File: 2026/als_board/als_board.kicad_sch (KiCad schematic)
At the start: 18 parts, among them J1 MAIN, J2 i2c, J3 PROG, U1 GM7333, U2 ME6209A50M3G, U3 CH32V003JxMx, U4 MAX485E

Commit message: ALS finishing touches
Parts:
- added R4, R5: 5k1, Resistor_SMD:R_0603_1608Metric, symbol Device:R_Small
- added R6, R7: 10k, Resistor_SMD:R_0603_1608Metric, symbol Device:R_Small
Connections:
- net +3V3: now also R6.1, R7.1
- net +5V: now also R4.1
- net GND: now also R5.2
- net SCL: now reaches J2.2 (Pin_2), U3.6 (PC2)
- net SCL: now also R6.2
- net SDA: now reaches J2.3 (Pin_3), U3.5 (PC1)
- net SDA: now also R7.2
- net at J1.3 (Pin_3), R3.1, U4.6 (A): now also R4.2
- net at J1.2 (Pin_2), R3.2, U4.7 (B): now also R5.1
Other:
- moved on the sheet: C5, C6, J1, J2, J3, R2, R3, U3, U4

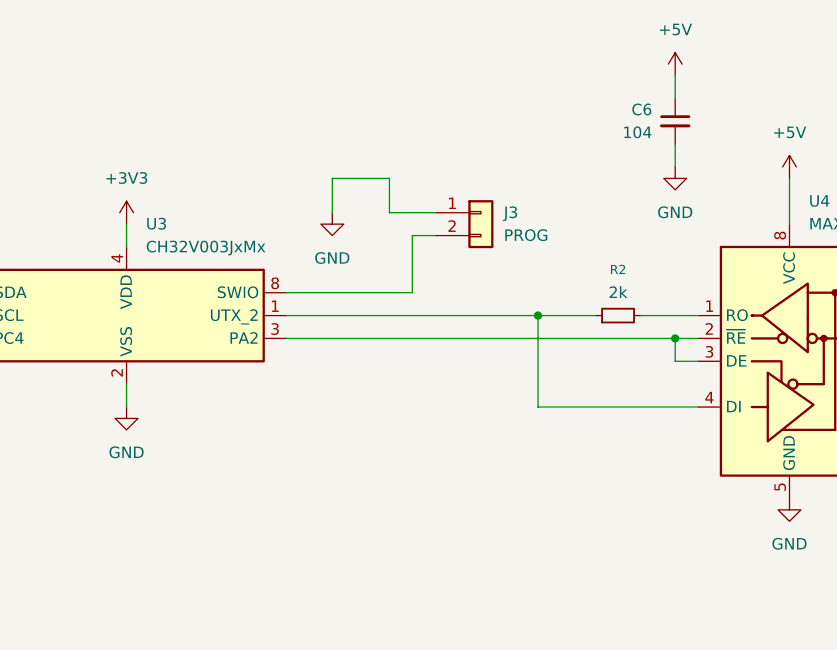
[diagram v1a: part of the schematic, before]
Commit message: ALS board with startup resistors for direction and output biasing (output off, high by default)
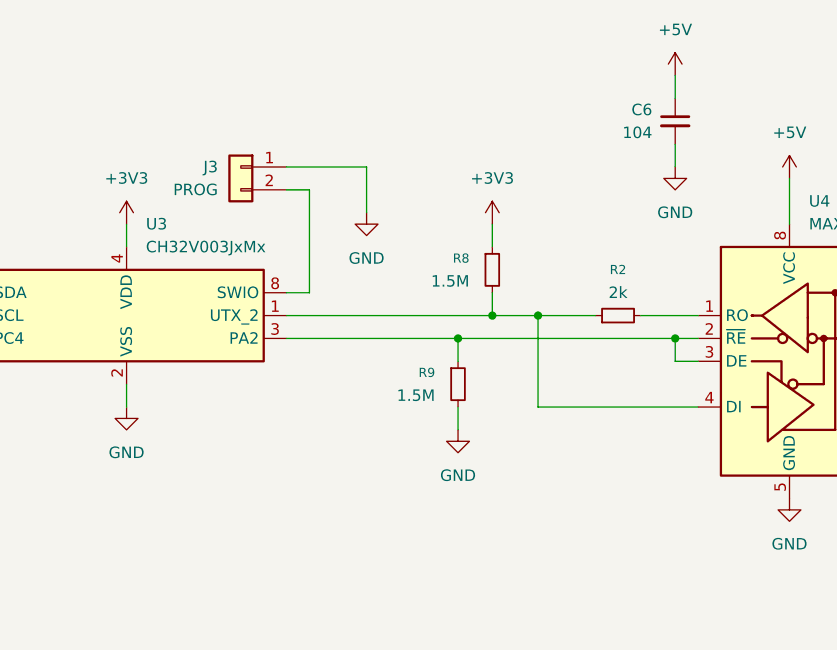
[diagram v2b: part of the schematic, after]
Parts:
- added R8, R9: 1.5M, Resistor_SMD:R_0603_1608Metric, symbol Device:R_Small
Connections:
- net +3V3: now also R8.1
- net GND: now also R9.2
- net at R2.1, U3.1 (PD6/PA1), U4.4 (DI): now also R8.2
- net at U3.3 (PA2), U4.2 (~{RE}), U4.3 (DE): now also R9.1
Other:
- moved on the sheet: J3

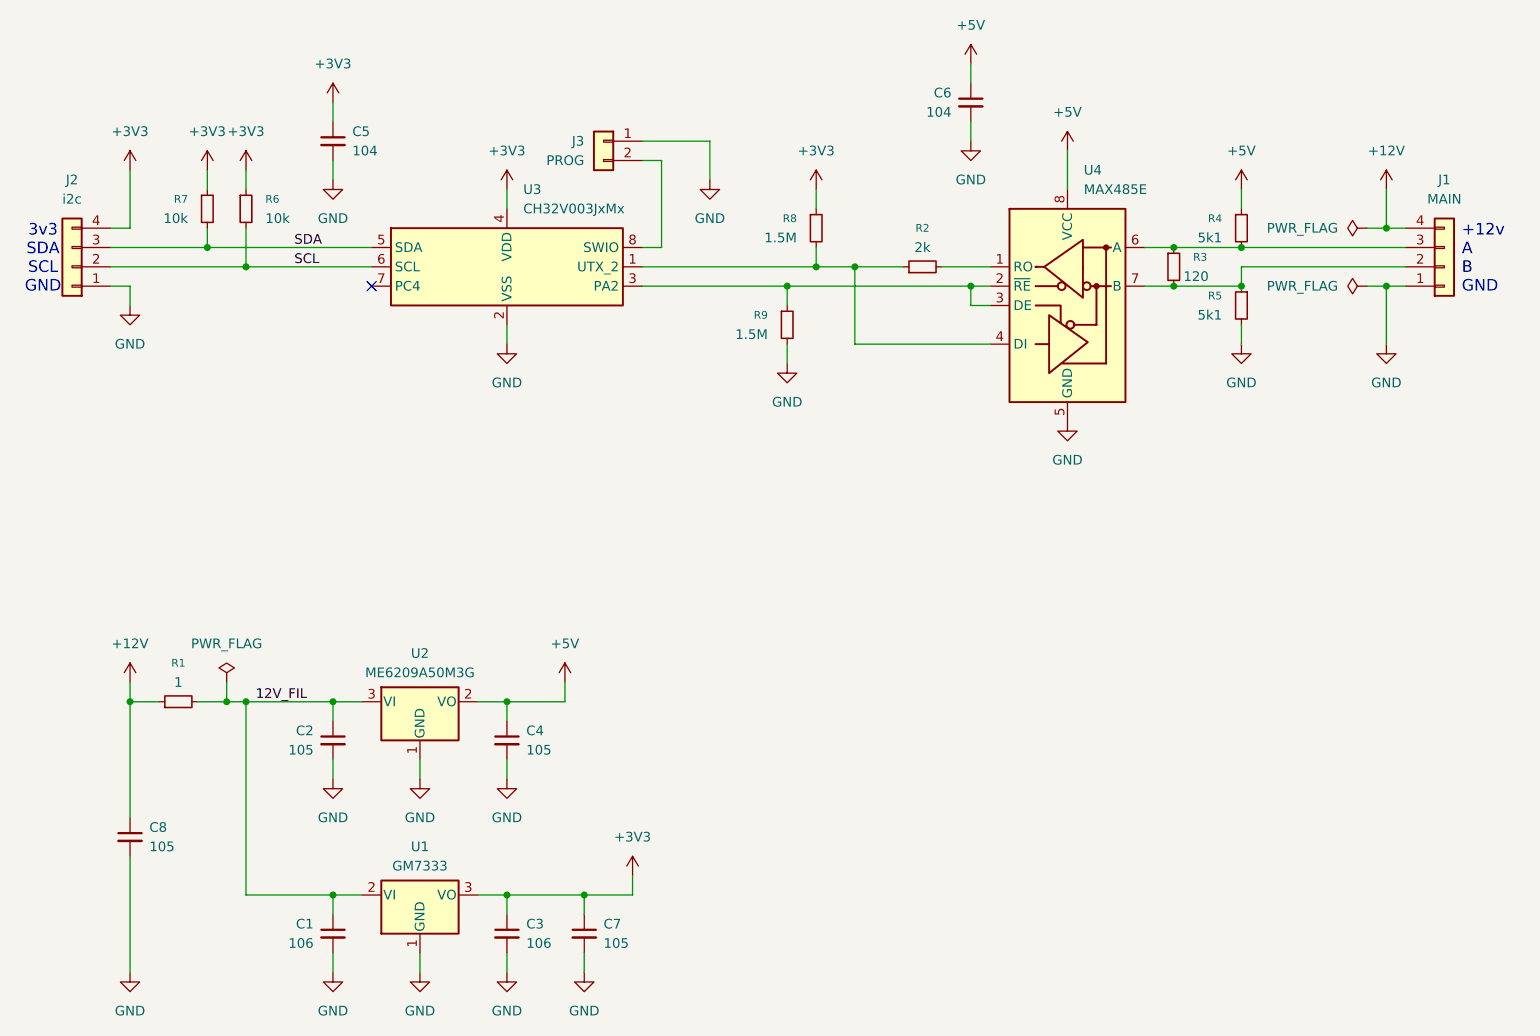
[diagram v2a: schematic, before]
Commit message: Ambient light sensor modification for better layout with better pad configuration and soldermasking
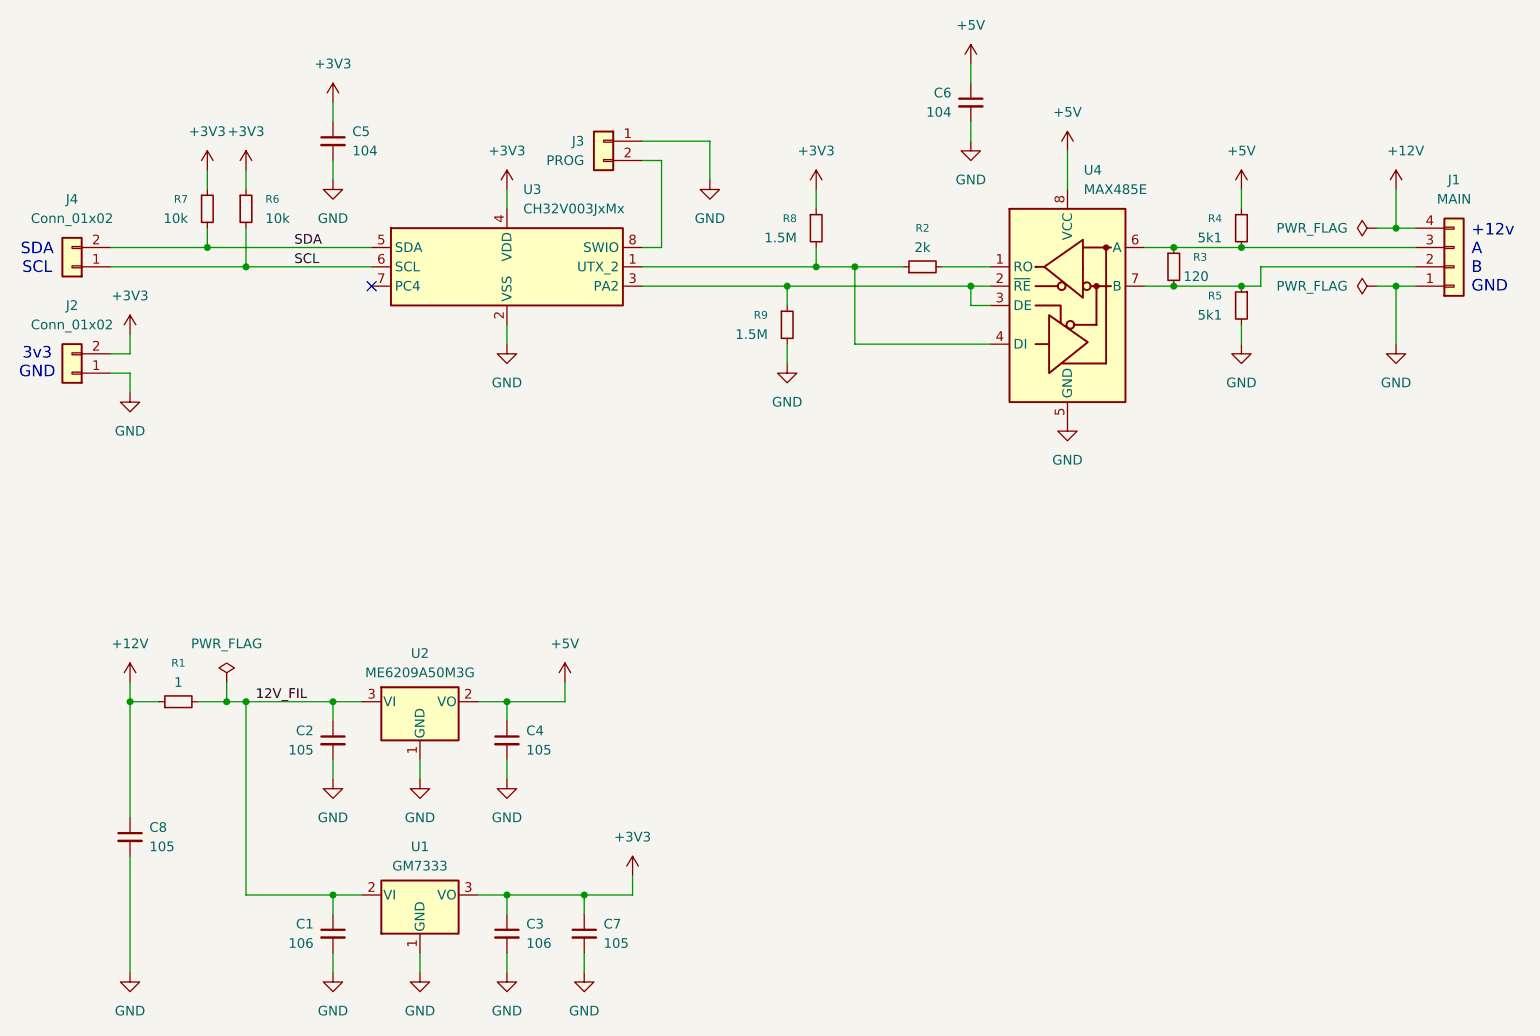
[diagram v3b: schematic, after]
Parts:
- removed J2: i2c, Connector_PinHeader_2.00mm:PinHeader_2x02_P2.00mm_Vertical_SMD, symbol Connector_Generic:Conn_01x04
- added J2: Conn_01x02, Resistor_SMD:R_1206_3216Metric, symbol Connector_Generic:Conn_01x02
- added J4: Conn_01x02, Resistor_SMD:R_0805_2012Metric, symbol Connector_Generic:Conn_01x02
- J1: footprint Connector_PinHeader_2.00mm:PinHeader_2x02_P2.00mm_Vertical_SMD -> this:PADS_4
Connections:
- net +3V3: now also J2.2 (Pin_2)
- net GND: now also J2.1 (Pin_1)
- net SCL: now also J4.1 (Pin_1)
- net SDA: now also J4.2 (Pin_2)
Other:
- note added: "3v3 GND"
- note added: "SDA SCL"
- note removed: "3v3 SDA SCL GND"
- moved on the sheet: J1
